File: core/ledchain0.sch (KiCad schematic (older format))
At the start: 60 parts, among them U10 WS2811, U11 WS2811, U12 WS2811, U13 WS2811, U14 WS2811, U15 WS2811, U16 WS2811, U17 WS2811, U18 WS2811, U19 WS2811, U2 WS2811, U20 WS2811, U21 WS2811, U22 WS2811, U23 WS2811, U24 WS2811, U25 WS2811, U26 WS2811, U27 WS2811, U28 WS2811, U29 WS2811, U30 WS2811, U31 WS2811, U32 WS2811, U4 WS2811, U5 WS2811, U6 WS2811, U7 WS2811, U8 WS2811, U9 WS2811

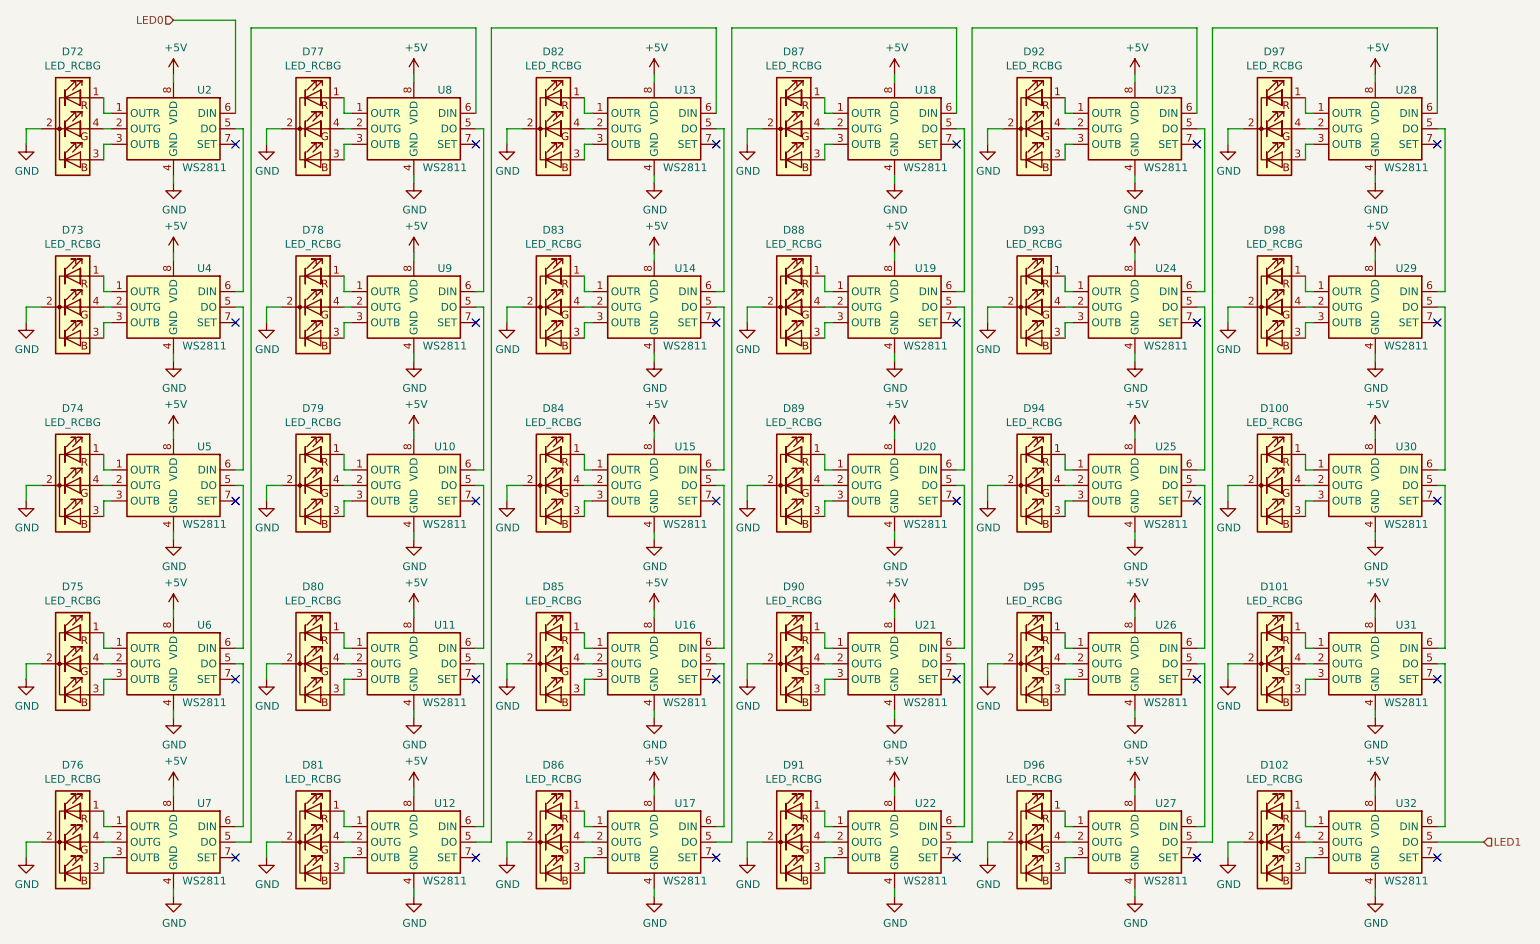
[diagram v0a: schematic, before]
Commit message: Fixed ERC errors and initially populated board
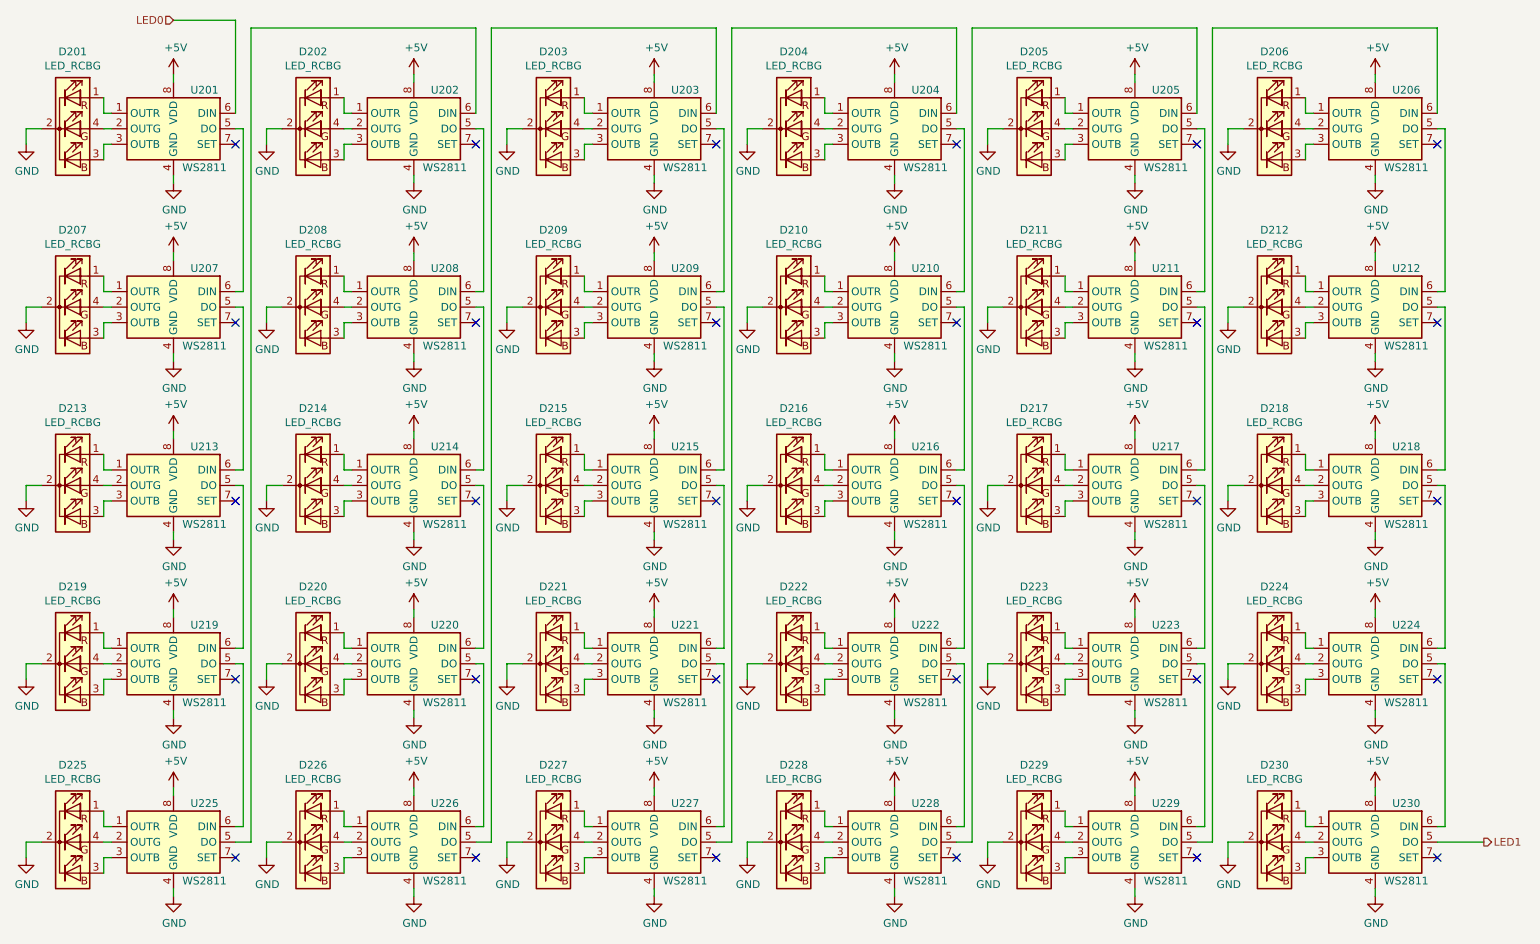
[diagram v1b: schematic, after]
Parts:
- renumbered D72 to D201, D77 to D202, D82 to D203, D87 to D204, D92 to D205, D97 to D206, D73 to D207, D78 to D208, D83 to D209, D88 to D210, D93 to D211, D98 to D212, D74 to D213, D79 to D214, D84 to D215, D89 to D216, D94 to D217, D100 to D218, D75 to D219, D80 to D220, D85 to D221, D90 to D222, D95 to D223, D101 to D224, D76 to D225, D81 to D226, D86 to D227, D91 to D228, D96 to D229, D102 to D230, U2 to U201, U8 to U202, U13 to U203, U18 to U204, U23 to U205, U28 to U206, U4 to U207, U9 to U208, U14 to U209, U19 to U210, U24 to U211, U29 to U212, U5 to U213, U10 to U214, U15 to U215, U20 to U216, U25 to U217, U30 to U218, U6 to U219, U11 to U220, U16 to U221, U21 to U222, U26 to U223, U31 to U224, U7 to U225, U12 to U226, U17 to U227, U22 to U228, U27 to U229, U32 to U230
